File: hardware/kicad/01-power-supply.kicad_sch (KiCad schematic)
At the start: 25 parts, among them J1 USB_C, J3 JST PH 2-pin, Q1 SI2301CDS, U2 IP5306, U3 AMS1117-3.3, U4 USBLC6-2SC6

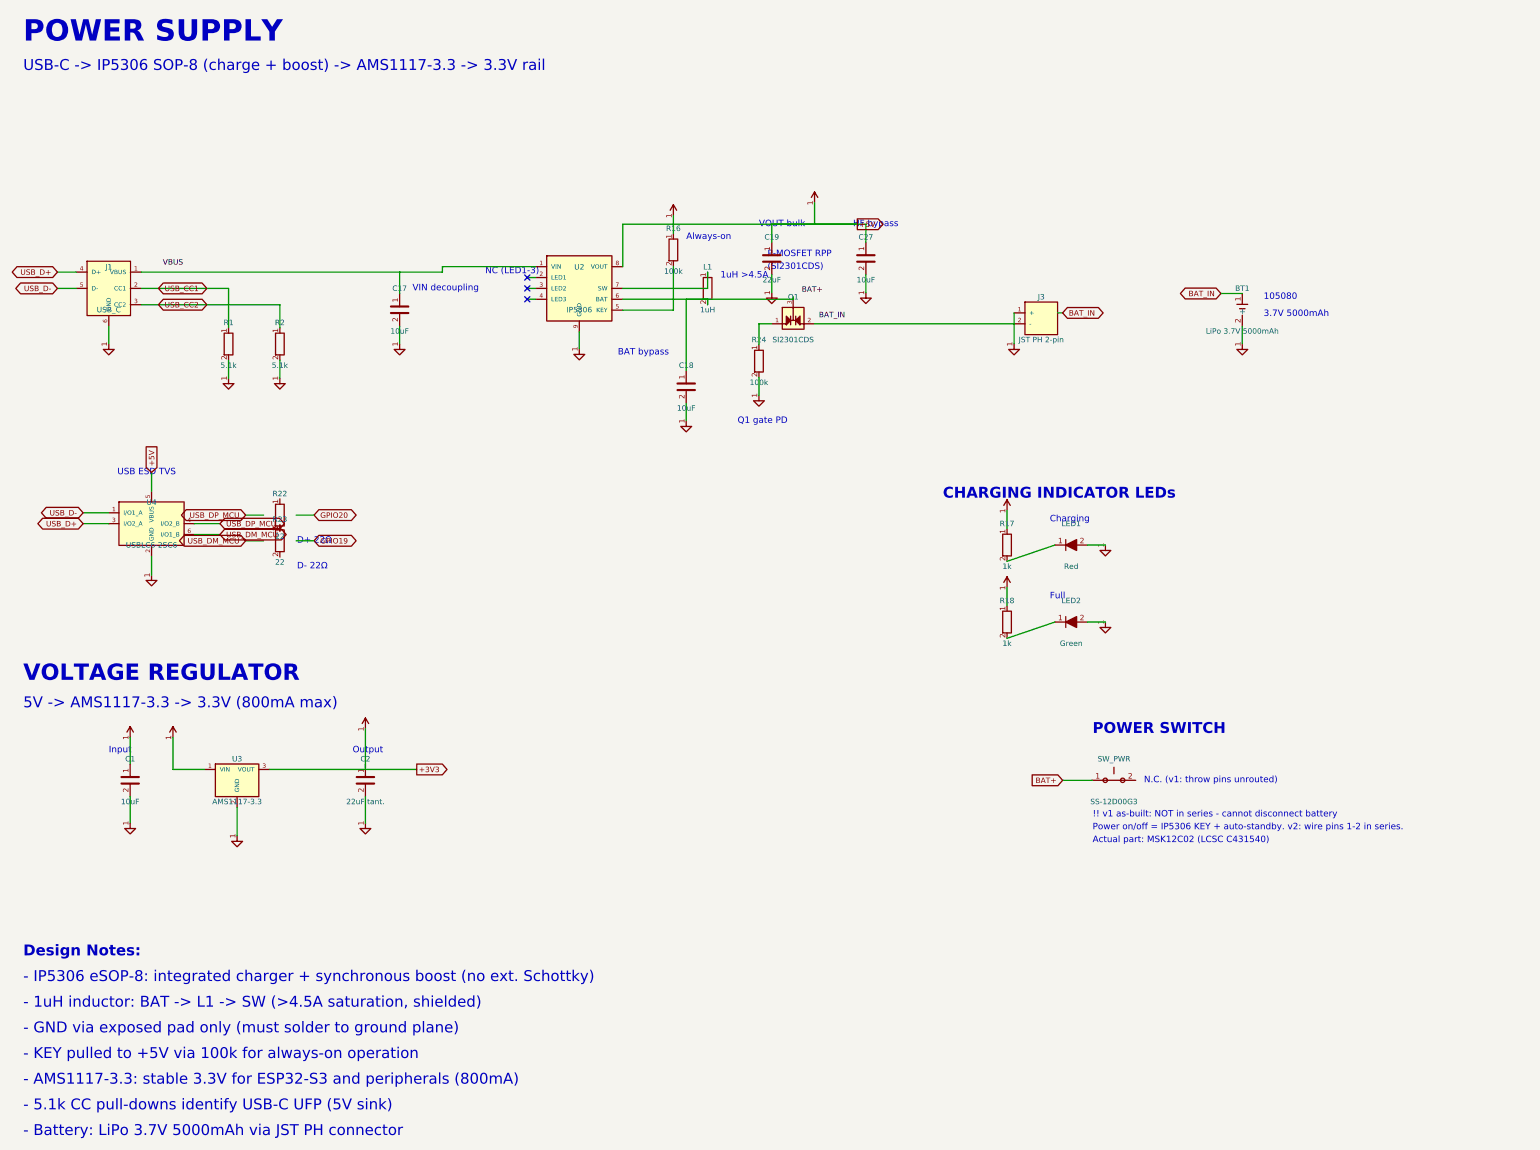
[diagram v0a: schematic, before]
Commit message: pwr(fix): un-split the +3V3 plane and replace the AMS1117 LDO with an SY8089 buck
Two changes to the power section, both in the same area of In2.Cu.

1. +3V3 split plane — this is why the v1 board could not boot.

The +5V pour on In2.Cu was a rectangle (105,35)-(140,65). It was far bigger
than the +5V copper needs and it swallowed every +3V3 via east of x=123: the
regulator output vias, the J4 display-power vias and the J4.29/34/35 pads.
Because a lower-priority zone is deleted where a higher-priority zone overlaps
it, those vias landed on +5V copper and connected to nothing. +3V3 resolved
into FOUR isolated electrical groups — a 4.92 mm2 regulator island at 3.3 V,
the main plane at 0 V, and two J4 orphans. The ESP32 never saw 3.3 V.

The PAM8403 +5V island (20,24)-(42,53) had the same defect on a smaller scale:
it trapped the R4 pull-up +3V3 via at (41.80, 44.50).

Fix: shrink both pours to the copper they actually need.
  zone #1  (105,35)-(140,65) -> (105,35)-(123,62)
  zone #2  (20,24)-(42,53)   -> (20,24)-(39.6,53)
  +5V PAM bridge via moved x=41.0 -> x=39.0 so it stays inside zone #2.
Every +5V feature is now at x<123 / y<62 with margin; nothing on +3V3 is
inside either pour.

  before: +3V3 = 4 groups, +5V = 1, GND = 1
  after:  +3V3 = 1 group,  +5V = 1, GND = 1

2. U3 AMS1117-3.3 (SOT-223) -> SY8089AAAC 2A synchronous buck (SOT-23-5,
   LCSC C78988).

The LDO burned (Vin-Vout) x Iload = 0.73 W at the 430 mA gaming load and ran
at Tj = 106 C. The buck burns the conversion loss only: 0.19 W, Tj = 73 C.
Vout = 0.6 x (1 + R25/R26) = 0.6 x (1 + 100k/22k) = 3.327 V.

New parts:
  L2  2.2uH  Sunlord SWPA4030S2R2MT (C36409), Isat 2.95 A, DCR 39 mOhm
  R25 100k / R26 22k   feedback divider
  C29 22pF             feed-forward across R25 (datasheet typical app)
  C30 22uF 1206 MLCC   C_OUT
  C1  10uF 0805 -> 22uF 1206 MLCC   C_IN (datasheet: >=10uF ceramic on IN)

C2 (22uF tantalum) is DELETED. It was the AMS1117 output cap, it is the part
that destroyed prototype #1 w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
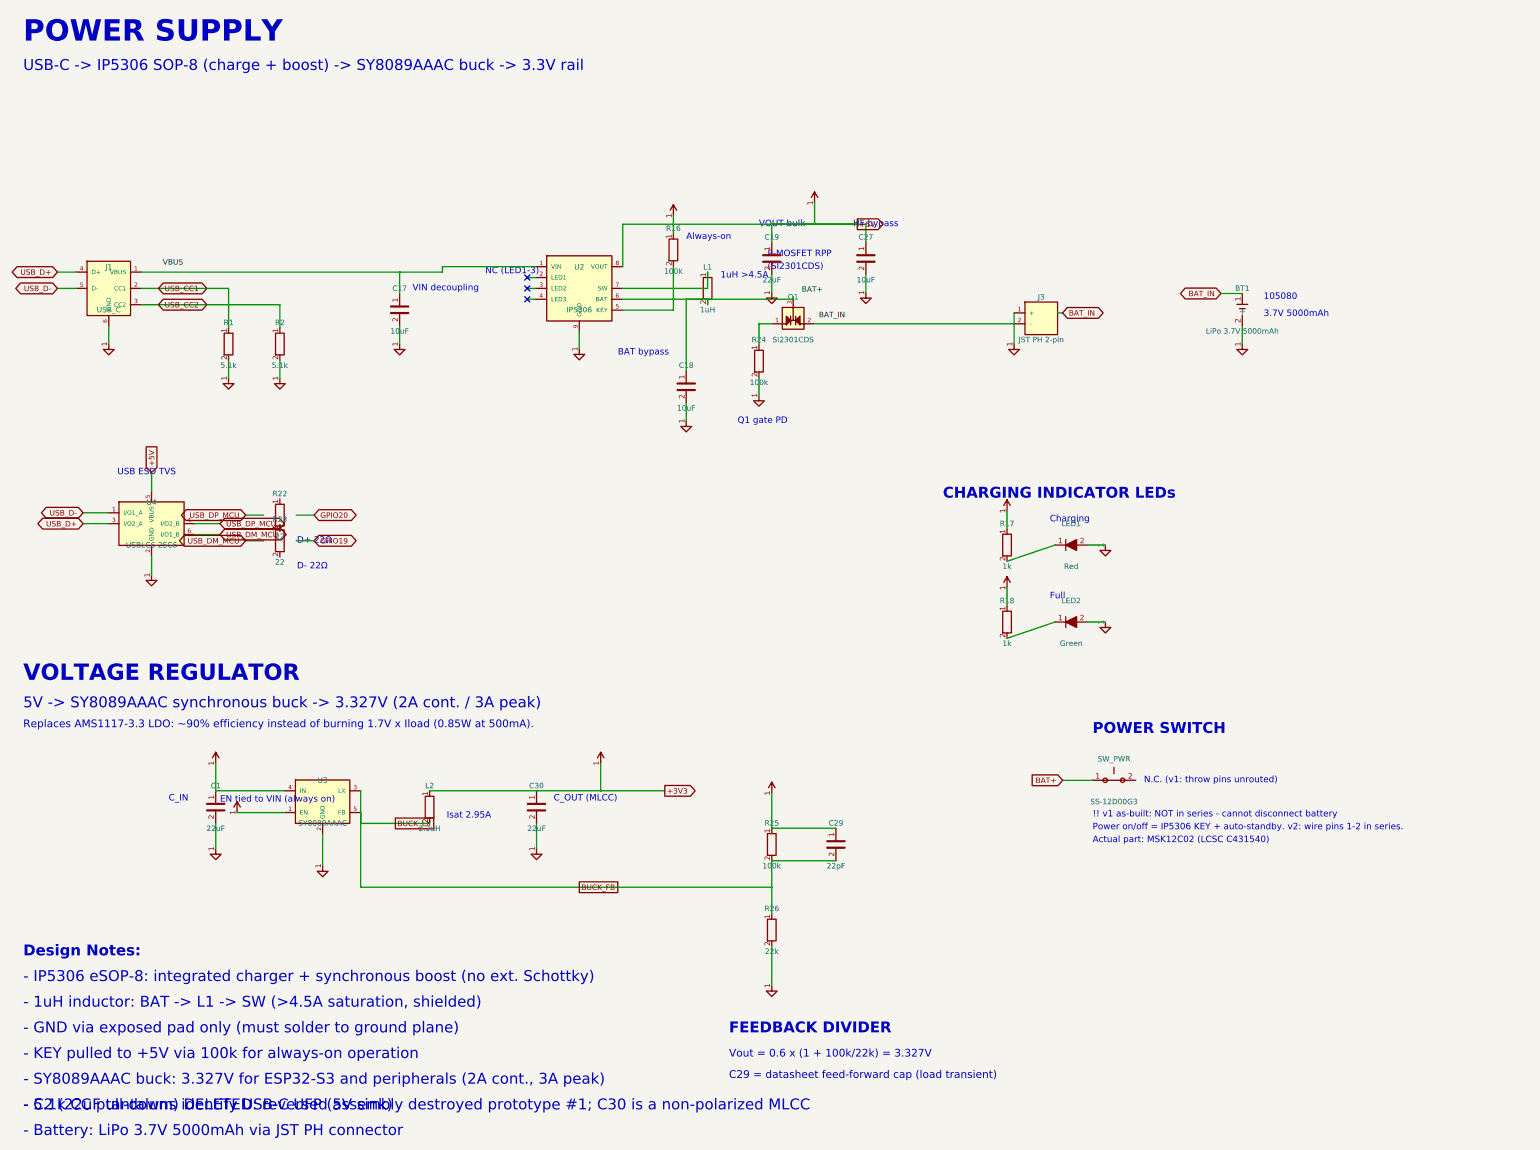
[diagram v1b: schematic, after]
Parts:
- removed C2: 22uF tant., symbol C
- removed U3: AMS1117-3.3, symbol AMS1117-3.3
- added C29: 22pF, symbol C
- added C30: 22uF, symbol C
- added L2: 2.2uH, symbol L
- added R25: 100k, symbol R
- added R26: 22k, symbol R
- added U3: SY8089AAAC, symbol SY8089AAAC
- C1: value 10uF -> 22uF
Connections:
- net +3V3: now also C30.1, L2.1
- net at C1.1: now also U3.4 (IN)
- new net: C29.1, R25.1
- new net BUCK_FB: C29.2, L2.2, R25.2, R26.1, U3.3 (LX), U3.5 (FB)
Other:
- note added: "- C2 (22uF tantalum) DELETED: reversed assembly destroyed prototype #1; C30 is a non-polarized MLCC"
- note added: "- SY8089AAAC buck: 3.327V for ESP32-S3 and peripherals (2A cont., 3A peak)"
- note added: "5V -> SY8089AAAC synchronous buck -> 3.327V (2A cont. / 3A peak)"
- note added: "C29 = datasheet feed-forward cap (load transient)"
- note added: "C_IN"
- note added: "C_OUT (MLCC)"
- note added: "EN tied to VIN (always on)"
- note added: "FEEDBACK DIVIDER"
- note added: "Isat 2.95A"
- note added: "Replaces AMS1117-3.3 LDO: ~90% efficiency instead of burning 1.7V x Iload (0.85W at 500mA)."
- note added: "USB-C -> IP5306 SOP-8 (charge + boost) -> SY8089AAAC buck -> 3.3V rail"
- note added: "Vout = 0.6 x (1 + 100k/22k) = 3.327V"
- note removed: "- AMS1117-3.3: stable 3.3V for ESP32-S3 and peripherals (800mA)"
- note removed: "5V -> AMS1117-3.3 -> 3.3V (800mA max)"
- note removed: "Input"
- note removed: "Output"
- note removed: "USB-C -> IP5306 SOP-8 (charge + boost) -> AMS1117-3.3 -> 3.3V rail"
- moved on the sheet: C1
